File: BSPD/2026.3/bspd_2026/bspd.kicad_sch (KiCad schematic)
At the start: 75 parts, among them J1 T2M-105-01-X-D-TH-DS, J2 39-30-6068, Q1 IRLIZ44N NMOS, U1 LM393, U2 4071 4 Channel 2 Input OR gate, U3 LM393, U4 LM393, U5 4081 AND Gate, U6 40106

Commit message: Update BSPD schematic and add BOM
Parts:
- C1, C2, C3, C4, C5, C6: Manufacturer_Name (none) -> Murata Electronics; Manufacturer_Part_Number (none) -> GRT188R71H104KE13D
- C10, C9: Manufacturer_Name (none) -> Murata Electronics; Manufacturer_Part_Number (none) -> GRM188R72E102KW07D
- C7: Manufacturer_Name (none) -> Kemet; Manufacturer_Part_Number (none) -> C0603C335K9PACTU
- C8: Manufacturer_Name (none) -> Murata Electronics; Manufacturer_Part_Number (none) -> GRM188R60J106KE47D
- D1, D2: Manufacturer_Name (none) -> Bourns Inc; Manufacturer_Part_Number (none) -> CD0603-B0240R
- J1: Manufacturer_Name (none) -> Samtec Inc.; Manufacturer_Part_Number (none) -> T2M-105-01-X-D-TH-DS
- Q1: Manufacturer_Name (none) -> Infineon; Manufacturer_Part_Number (none) -> IRLZ44NPBF
- R1, R11, R12, R13, R22, R23, R24, R4, R5, R9: Manufacturer_Name (none) -> Yageo; Manufacturer_Part_Number (none) -> RC0603FR-0720KL
- R10, R16, R17, R2, R3, R6, R7, R8: Manufacturer_Name (none) -> Yageo; Manufacturer_Part_Number (none) -> RC0603FR-0710KL
- R14: Manufacturer_Name (none) -> Yageo; Manufacturer_Part_Number (none) -> RC0603FR-07120KL
- R15, R19, R20: Manufacturer_Name (none) -> Yageo; Manufacturer_Part_Number (none) -> RC0603FR-071KL
- R18, R21: Manufacturer_Name (none) -> Yageo; Manufacturer_Part_Number (none) -> RC0603FR-07500KL
- R_Bypass1, R_Bypass2: Manufacturer_Name (none) -> Yageo
- U1, U3, U4: Manufacturer_Name (none) -> Texas Instruments; Manufacturer_Part_Number (none) -> LM393P
- U2: Manufacturer_Name (none) -> Texas Instruments; Manufacturer_Part_Number (none) -> CD4071BE
- U5: Manufacturer_Name (none) -> Texas Instruments; Manufacturer_Part_Number (none) -> CD4081BEE4
- U6: value 40106 -> 40106 Inverter; Manufacturer_Name (none) -> Texas Instruments; Manufacturer_Part_Number (none) -> CD40106BE

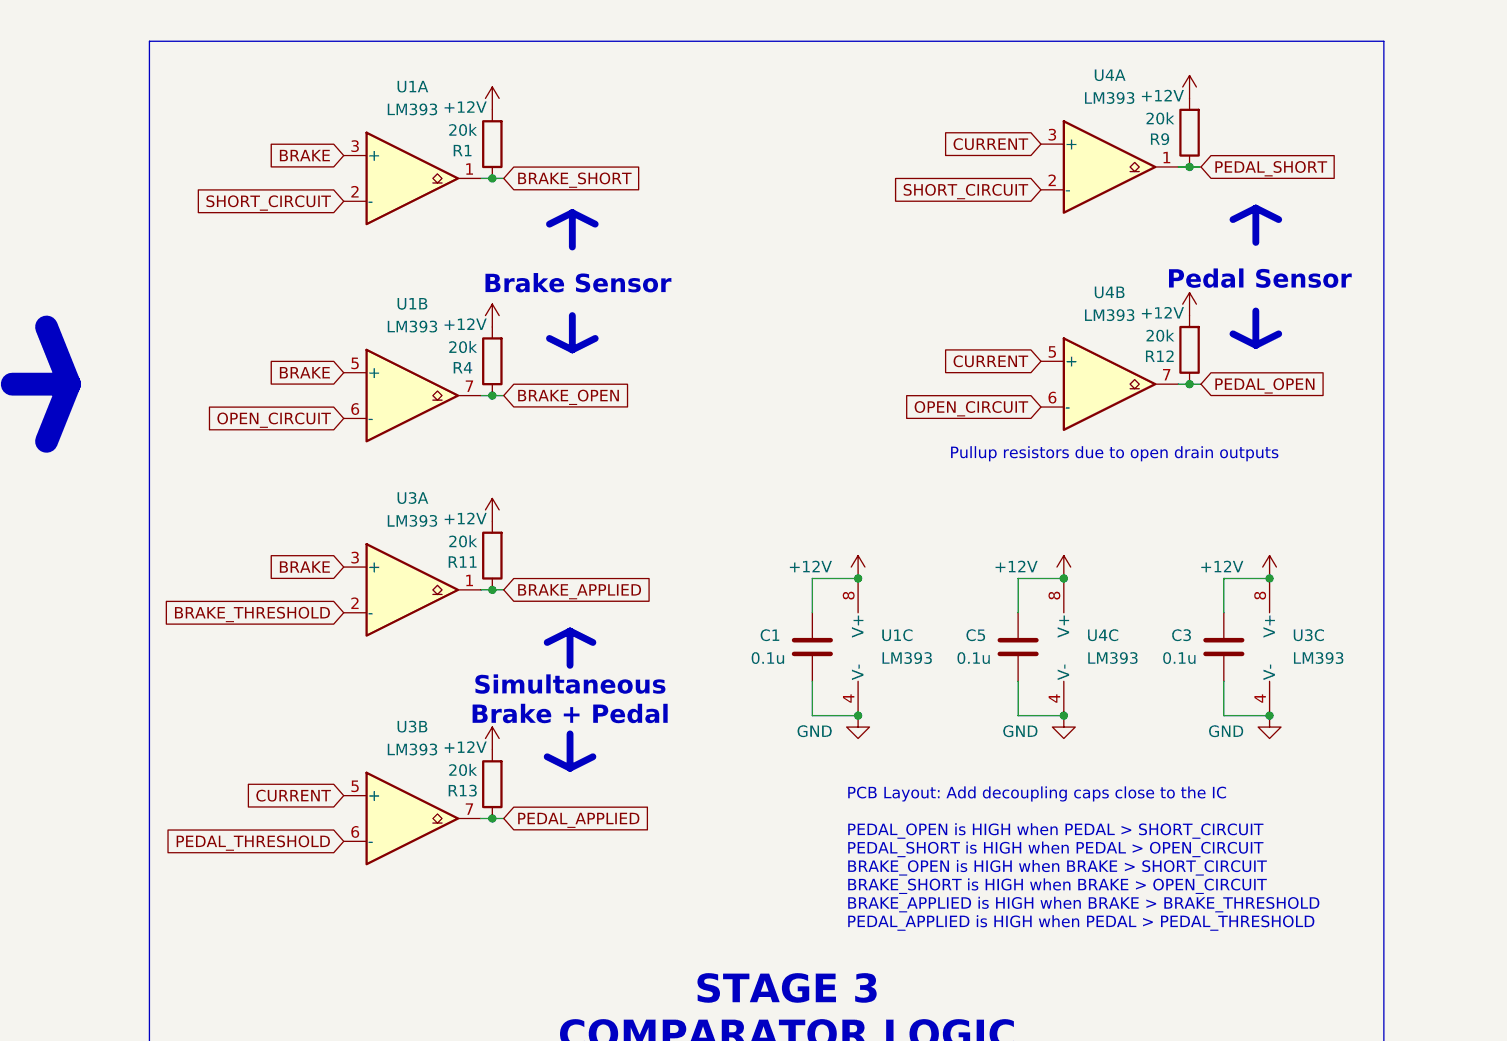
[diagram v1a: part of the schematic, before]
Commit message: fixed comparator pinouts and pcb layout
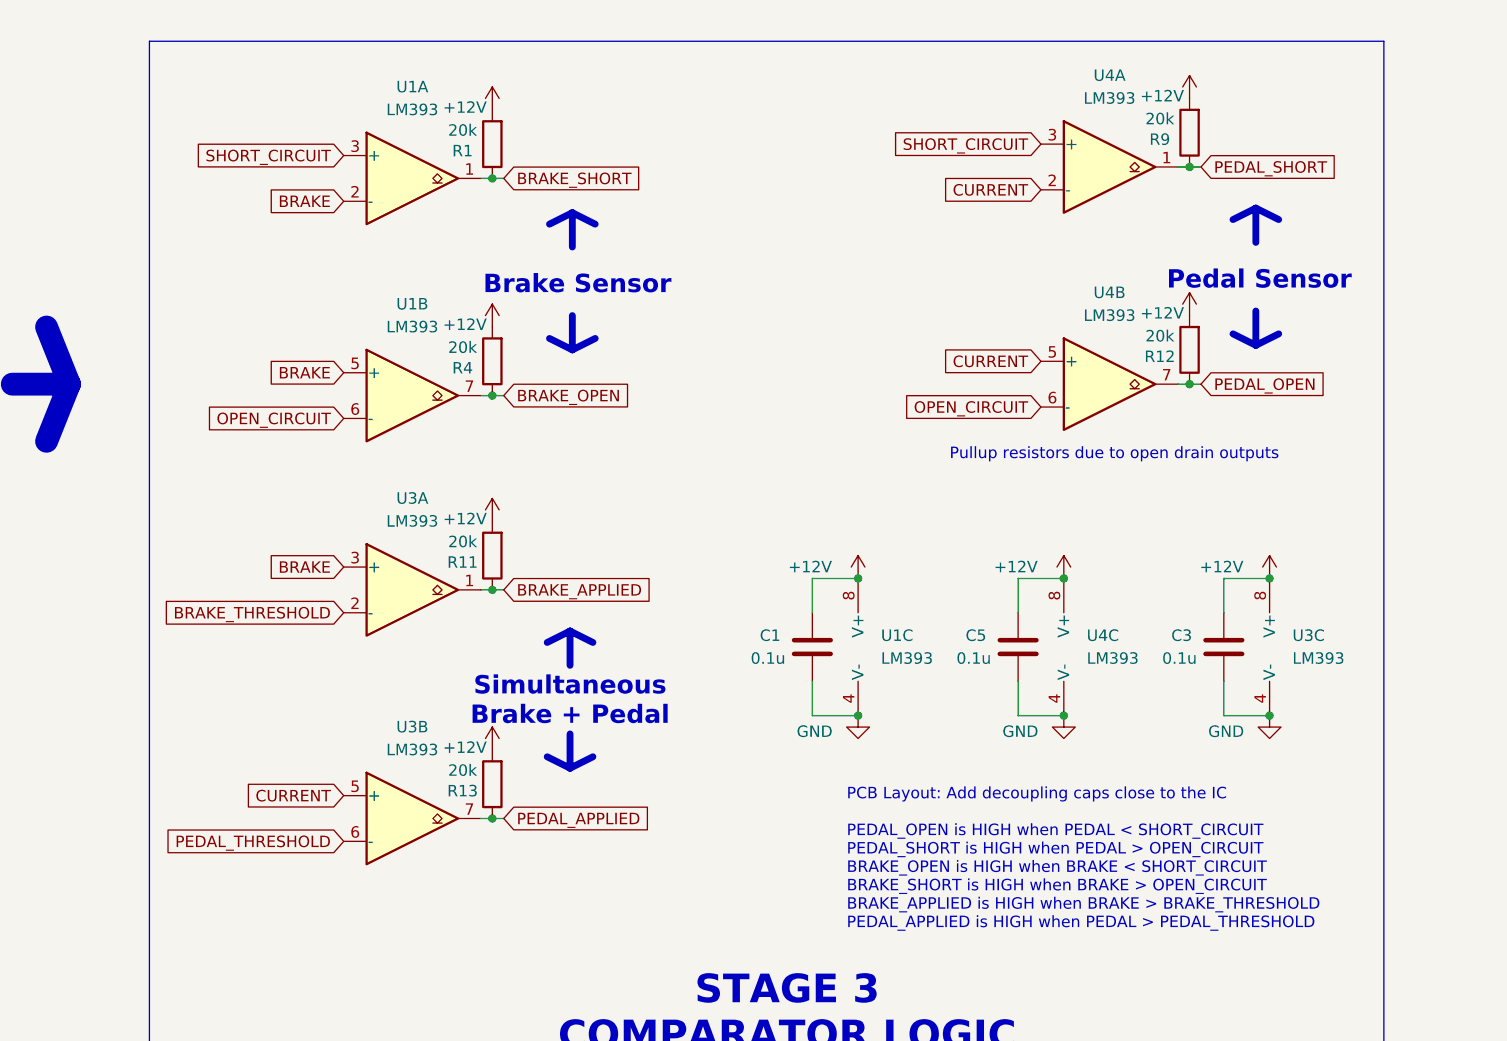
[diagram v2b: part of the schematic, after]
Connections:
- net BRAKE: now also U1.2 (-); no longer U1.3 (+)
- net CURRENT: now also U4.2 (-); no longer U4.3 (+)
- net SHORT_CIRCUIT: now also U1.3 (+), U4.3 (+); no longer U1.2 (-), U4.2 (-)
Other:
- note added: "PCB Layout: Add decoupling caps close to the IC PEDAL_OPEN is HIGH when PEDAL < SHORT_CIRCUIT PEDAL_SHORT is HIGH when PEDAL > OPEN_CIRCUIT BRAKE_OPEN is HIGH when BRAKE < SHORT_CIRCUIT BRAKE_SHORT is HIGH when BRAKE > OPEN_CIRCUIT BRAKE_APPLIED is HIGH when BRAKE > BRAKE_THRESHOLD PEDAL_APPLIED is HIGH when PEDAL > PEDAL_THRESHOLD"
- note removed: "PCB Layout: Add decoupling caps close to the IC PEDAL_OPEN is HIGH when PEDAL > SHORT_CIRCUIT PEDAL_SHORT is HIGH when PEDAL > OPEN_CIRCUIT BRAKE_OPEN is HIGH when BRAKE > SHORT_CIRCUIT BRAKE_SHORT is HIGH when BRAKE > OPEN_CIRCUIT BRAKE_APPLIED is HIGH when BRAKE > BRAKE_THRESHOLD PEDAL_APPLIED is HIGH when PEDAL > PEDAL_THRESHOLD"
